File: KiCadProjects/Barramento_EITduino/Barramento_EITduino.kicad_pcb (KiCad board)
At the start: 2 copper layers, 90 x 100 mm, 3 parts, among them J2 tensoes, J3 sinais analogicos, J4 comunicacao / sinais digitais

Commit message: Descrição do barramento: esquemático
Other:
- board text added: "VCC"
- board text added: "VEE"
- board text removed: "+12V"
- board text removed: "-12V"
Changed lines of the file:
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@@
   (gr_line (start 101.6 50.8) (end 101.6 150.7998)
     (stroke (width 0.5) (type default)) (layer "Edge.Cuts"))
-  (gr_text "SDA1" (at 177.8 144.78) (layer "F.Cu")
+  (gr_text "SDA1" (at 178.816 144.5) (layer "F.Cu")
     (effects (font (size 1.5 1.5) (thickness 0.3) bold) (justify left bottom))
   )
-  (gr_text "SinA" (at 109.22 144.78) (layer "F.Cu")
+  (gr_text "SinA" (at 108.712 145.796) (layer "F.Cu")
     (effects (font (size 1.5 1.5) (thickness 0.3) bold) (justify left bottom))
   )
-  (gr_text "SPI_CIPO\n" (at 172.72 63.5) (layer "F.Cu")
+  (gr_text "SPI_CIPO\n" (at 174.45 63.35) (layer "F.Cu")
     (effects (font (size 1.5 1.5) (thickness 0.3) bold) (justify left bottom))
   )
-  (gr_text "CS_x9c10x\n" (at 172.72 71.12) (layer "F.Cu")
+  (gr_text "CS_x9c10x\n" (at 172.35 70.75) (layer "F.Cu")
     (effects (font (size 1.5 1.5) (thickness 0.3) bold) (justify left bottom))
   )
-  (gr_text "-9V" (at 109.22 68.58) (layer "F.Cu")
+  (gr_text "-9V" (at 108.55 68.4) (layer "F.Cu")
     (effects (font (size 1.5 1.5) (thickness 0.3) bold) (justify left bottom))
   )
-  (gr_text "CS_ad9833" (at 172.72 68.58) (layer "F.Cu")
+  (gr_text "CS_ad9833" (at 172.1 68.3) (layer "F.Cu")
     (effects (font (size 1.5 1.5) (thickness 0.3) bold) (justify left bottom))
   )
-  (gr_text "+3.3V" (at 109.22 76.2) (layer "F.Cu")
+  (gr_text "+3.3V" (at 108.55 76) (layer "F.Cu")
     (effects (font (size 1.5 1.5) (thickness 0.3) bold) (justify left bottom))
   )
-  (gr_text "Sin1" (at 109.22 139.7) (layer "F.Cu")
+  (gr_text "Sin1" (at 108.7 140.9) (layer "F.Cu")
     (effects (font (size 1.5 1.5) (thickness 0.3) bold) (justify left bottom))
   )
-  (gr_text "+5V\n" (at 109.22 71.12) (layer "F.Cu")
+  (gr_text "+5V\n" (at 108.6 70.9) (layer "F.Cu")
     (effects (font (size 1.5 1.5) (thickness 0.3) bold) (justify left bottom))
   )
-  (gr_text "SCL2" (at 177.8 137.16) (layer "F.Cu")
+  (gr_text "SCL2" (at 178.816 136.95) (layer "F.Cu")
     (effects (font (size 1.5 1.5) (thickness 0.3) bold) (justify left bottom))
   )
-  (gr_text "-5V" (at 109.22 73.66) (layer "F.Cu")
+  (gr_text "-5V" (at 108.6 73.45) (layer "F.Cu")
     (effects (font (size 1.5 1.5) (thickness 0.3) bold) (justify left bottom))
   )
-  (gr_text "GND" (at 109.22 58.42) (layer "F.Cu")
+  (gr_text "GND" (at 108.6 58.1) (layer "F.Cu")
     (effects (font (size 1.5 1.5) (thickness 0.3) bold) (justify left bottom))
   )
-  (gr_text "SDA3" (at 177.8 134.62) (layer "F.Cu")
+  (gr_text "SDA3" (at 178.816 134.4) (layer "F.Cu")
     (effects (font (size 1.5 1.5) (thickness 0.3) bold) (justify left bottom))
   )
-  (gr_text "Ampl2" (at 109.22 137.16) (layer "F.Cu")
+  (gr_text "Ampl2" (at 108.712 138.176) (layer "F.Cu")
     (effects (font (size 1.5 1.5) (thickness 0.3) bold) (justify left bottom))
   )
-  (gr_text "SINC" (at 177.8 58.42) (layer "F.Cu")
+  (gr_text "SINC" (at 179.2 58.2) (layer "F.Cu")
     (effects (font (size 1.5 1.5) (thickness 0.3) bold) (justify left bottom))
   )
-  (gr_text "+12V\n" (at 109.22 60.96) (layer "F.Cu")
+  (gr_text "VCC" (at 108.75 60.55) (layer "F.Cu")
     (effects (font (size 1.5 1.5) (thickness 0.3) bold) (justify left bottom))
   )
-  (gr_text "-12V\n" (at 109.22 63.5) (layer "F.Cu")
+  (gr_text "VEE\n" (at 108.8 63.15) (layer "F.Cu")
     (effects (font (size 1.5 1.5) (thickness 0.3) bold) (justify left bottom))
   )
-  (gr_text "I2\n" (at 109.22 132.08) (layer "F.Cu")
+  (gr_text "I2\n" (at 108.7 133.15) (layer "F.Cu")
     (effects (font (size 1.5 1.5) (thickness 0.3) bold) (justify left bottom))
   )
-  (gr_text "SinB" (at 109.22 147.32) (layer "F.Cu")
+  (gr_text "SinB" (at 108.7 148.45) (layer "F.Cu")
     (effects (font (size 1.5 1.5) (thickness 0.3) bold) (justify left bottom))
   )
-  (gr_text "SDA2" (at 177.8 139.7) (layer "F.Cu")
+  (gr_text "SDA2" (at 178.816 139.4) (layer "F.Cu")
     (effects (font (size 1.5 1.5) (thickness 0.3) bold) (justify left bottom))
   )
-  (gr_text "SPI_clk\n" (at 172.72 66.04) (layer "F.Cu")
+  (gr_text "SPI_clk\n" (at 176.45 65.8) (layer "F.Cu")
     (effects (font (size 1.5 1.5) (thickness 0.3) bold) (justify left bottom))
   )
-  (gr_text "I1" (at 109.22 129.54) (layer "F.Cu")
+  (gr_text "I1" (at 108.712 130.556) (layer "F.Cu")
     (effects (font (size 1.5 1.5) (thickness 0.3) bold) (justify left bottom))
   )
-  (gr_text "Sin2\n" (at 109.22 142.24) (layer "F.Cu")
+  (gr_text "Sin2\n" (at 108.7 143.35) (layer "F.Cu")
     (effects (font (size 1.5 1.5) (thickness 0.3) bold) (justify left bottom))
   )
-  (gr_text "+9V\n" (at 109.22 66.04) (layer "F.Cu")
+  (gr_text "+9V\n" (at 108.6 65.75) (layer "F.Cu")
     (effects (font (size 1.5 1.5) (thickness 0.3) bold) (justify left bottom))
   )
-  (gr_text "SCL1\n" (at 177.8 142.24) (layer "F.Cu")
+  (gr_text "SCL1\n" (at 178.816 141.94) (layer "F.Cu")
     (effects (font (size 1.5 1.5) (thickness 0.3) bold) (justify left bottom))
   )
-  (gr_text "SPI_COPI\n" (at 172.72 60.96) (layer "F.Cu")
+  (gr_text "SPI_COPI\n" (at 174.45 60.8) (layer "F.Cu")
     (effects (font (size 1.5 1.5) (thickness 0.3) bold) (justify left bottom))
   )
-  (gr_text "SCL3" (at 177.8 132.08) (layer "F.Cu")
+  (gr_text "SCL3" (at 178.816 131.9) (layer "F.Cu")
     (effects (font (size 1.5 1.5) (thickness 0.3) bold) (justify left bottom))
   )
-  (gr_text "Ampl1" (at 109.22 134.62) (layer "F.Cu")
+  (gr_text "Ampl1" (at 108.712 135.636) (layer "F.Cu")
     (effects (font (size 1.5 1.5) (thickness 0.3) bold) (justify left bottom))
   )

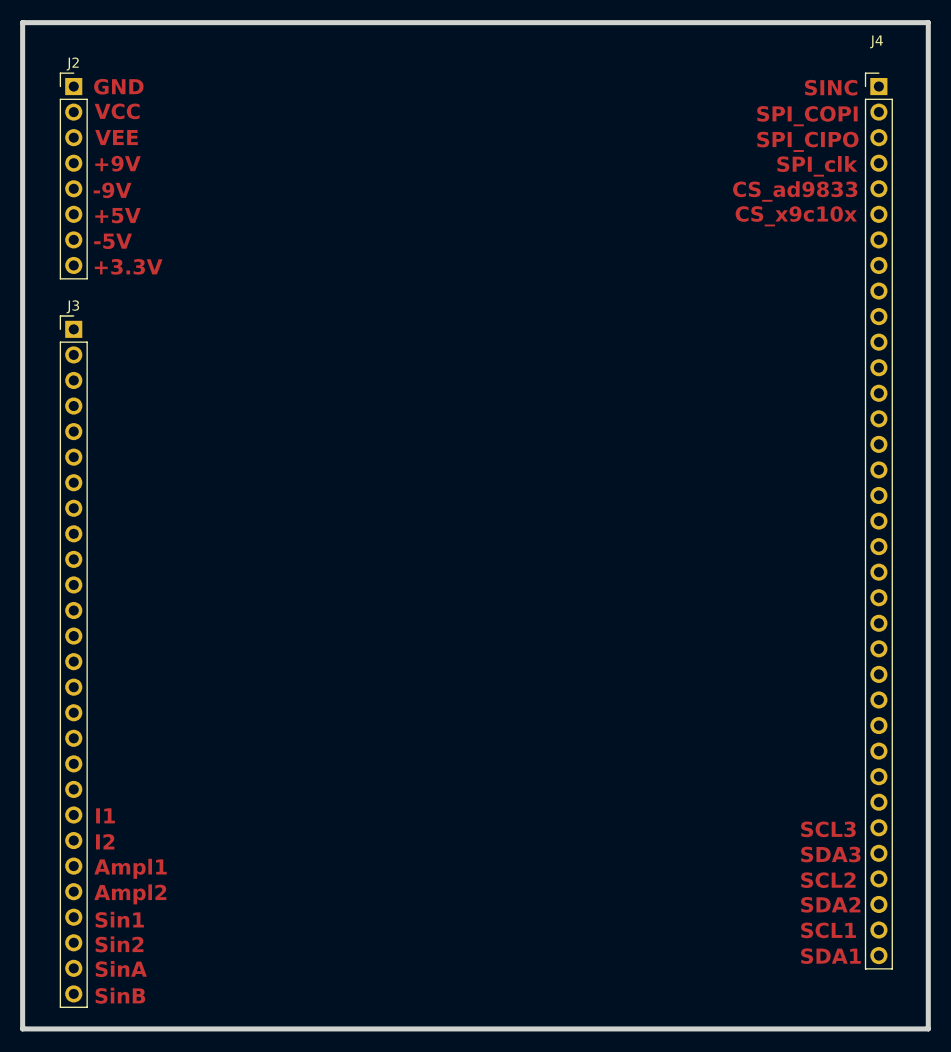
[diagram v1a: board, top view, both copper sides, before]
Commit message: arquivos para fabricar a base
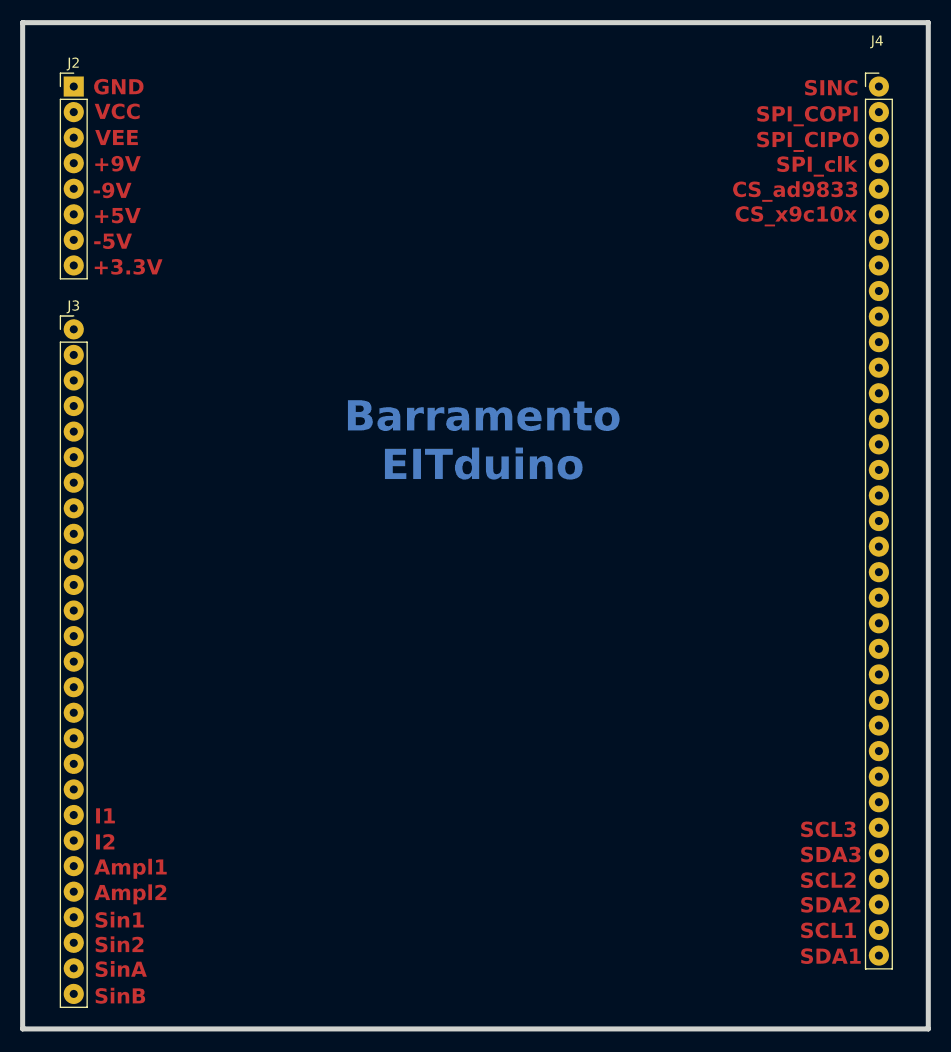
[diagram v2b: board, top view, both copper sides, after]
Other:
- board text added: "Barramento EITduino"
